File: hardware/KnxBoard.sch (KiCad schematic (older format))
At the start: 40 parts, among them J1 Conn_01x10, J2 Conn_01x12, J3 Conn_01x12, J4 Conn_01x02_Male, U1 NCN5130, U2 STM32L432KCUx, X1 FA-238

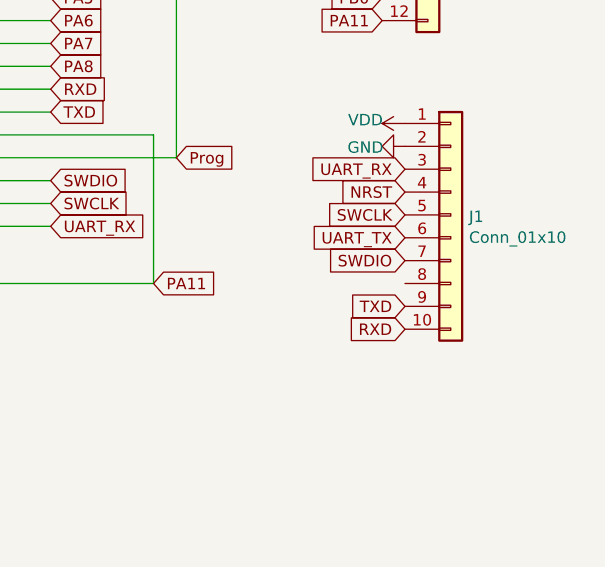
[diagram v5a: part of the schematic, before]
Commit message: update BOM prices by 10
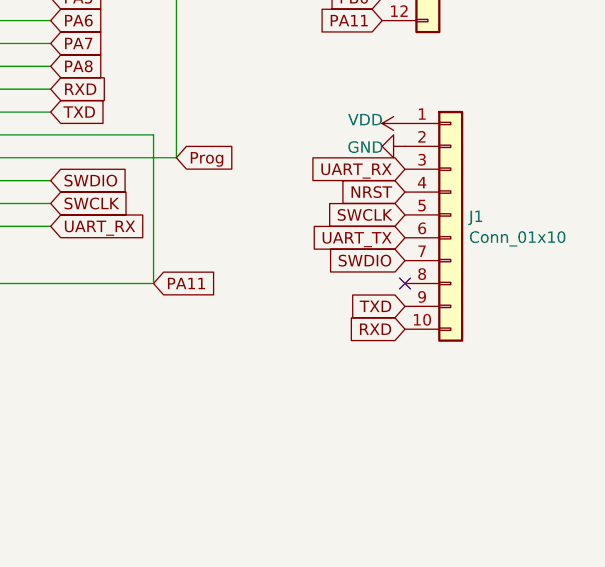
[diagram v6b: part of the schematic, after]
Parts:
- C1: Price 0.085 -> 0.021
- C10, C11, C22: Price 0.093 -> 0.039
- C2: Price 0.136 -> 0.097
- C20, C21, C23, C5, C6: Price 0.085 -> 0.026
- C3: Price 0.09 -> 0.014
- C4: Price 0.46 -> 0.353
- C41: Price 0.14 -> 0.102
- C8, C9: Price 0.085 -> 0.032
- D1: Price 0.36 -> 0.292
- D2: Price 0.3 -> 0.249
- L1, L2, L3: Price 0.15 -> 0.109
- LD1: Price 0.152 -> 0.142
- R1: Price 0.382 -> 0.285
- R22: value 0 -> NOTMOUNT
- U1: Price 7.31 -> 6.61
- U2: Price 5.8 -> 5.22
- X1: Price 0.53 -> 0.445
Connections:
- no-connect marks 2 -> 3
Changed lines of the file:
@@
 F 2 "Package_DFN_QFN:QFN-32-1EP_5x5mm_P0.5mm_EP3.45x3.45mm" H 8150 2700 50  0001 R CNN
 F 3 "https://www.mouser.fr/ProductDetail/STMicroelectronics/STM32L432KCU6?qs=sGAEpiMZZMueQxo7L%2FBPyGlkDlHQ8XwjqFkWSLh2yvA%3D" H 8550 3600 50  0001 C CNN
-F 4 "5.8" H 8550 3600 50  0001 C CNN "Price"
+F 4 "5.22" H 8550 3600 50  0001 C CNN "Price"
 	1    8550 3600
 	1    0    0    -1
@@
 F 2 "Package_DFN_QFN:QFN-40-1EP_6x6mm_P0.5mm_EP4.6x4.6mm_ThermalVias" H 3500 5300 50  0001 C CNN
 F 3 "https://www.mouser.fr/ProductDetail/onsemi/NCN5130MNTWG?qs=sGAEpiMZZMsyYdr3R27aV%2FyfBetTZLuYah%252BU%2FGK00PQ%3D" H 3150 3650 50  0001 C CNN
-F 4 "7.31" H 3150 3650 50  0001 C CNN "Price"
+F 4 "6.61" H 3150 3650 50  0001 C CNN "Price"
 	1    3150 3650
 	1    0    0    -1
@@
 F 2 "Diode_SMD:D_SMA" H 1150 3750 50  0001 C CNN
 F 3 "https://www.mouser.fr/ProductDetail/Bourns/SMAJ40CA?qs=A3H9pljuJ8S9ch8FWCUIag%3D%3D" H 1150 3750 50  0001 C CNN
-F 4 "0.3" H 1150 3750 50  0001 C CNN "Price"
+F 4 "0.249" H 1150 3750 50  0001 C CNN "Price"
 	1    1150 3750
 	0    1    1    0
@@
 F 2 "Diode_SMD:D_SMA" H 1400 3200 50  0001 C CNN
 F 3 "https://www.mouser.fr/ProductDetail/onsemi/SS16T3G?qs=xZq1yRCsb1c8788h1nFazA%3D%3D" H 1400 3200 50  0001 C CNN
-F 4 "0.36" H 1400 3200 50  0001 C CNN "Price"
+F 4 "0.292" H 1400 3200 50  0001 C CNN "Price"
 	1    1400 3200
 	-1   0    0    1
@@
 F 2 "Resistor_SMD:R_0612_1632Metric" V 2180 3200 50  0001 C CNN
 F 3 "https://www.mouser.fr/ProductDetail/KOA-Speer/WK73R2BTTD27R0F?qs=sGAEpiMZZMvdGkrng054t6odK5HnpZ6cfyF1%252BzoyWdM%3D" H 2250 3200 50  0001 C CNN
-F 4 "0.382" H 2250 3200 50  0001 C CNN "Price"
+F 4 "0.285" H 2250 3200 50  0001 C CNN "Price"
 	1    2250 3200
 	0    1    1    0
@@
 F 2 "Capacitor_SMD:C_0603_1608Metric" H 1988 3150 50  0001 C CNN
 F 3 "https://www.mouser.fr/ProductDetail/Samsung-Electro-Mechanics/CL10B473KB8NNND?qs=sGAEpiMZZMvsSlwiRhF8qlxW52pIu5FNnJM8feowB3A%3D" H 1950 3300 50  0001 C CNN
-F 4 "0.085" H 1950 3300 50  0001 C CNN "Price"
+F 4 "0.021" H 1950 3300 50  0001 C CNN "Price"
 	1    1950 3300
 	0    1    1    0
@@
 F 2 "Capacitor_SMD:C_0603_1608Metric" H 2338 3450 50  0001 C CNN
 F 3 "https://www.mouser.fr/ProductDetail/Samsung-Electro-Mechanics/CL10A224KB8NNNC?qs=sGAEpiMZZMvsSlwiRhF8qtsGU%2FCnaNeQ2pAx%2FyO8BDlqGcrTKW51Mg%3D%3D" H 2300 3600 50  0001 C CNN
-F 4 "0.136" H 2300 3600 50  0001 C CNN "Price"
+F 4 "0.097" H 2300 3600 50  0001 C CNN "Price"
 	1    2300 3600
 	0    1    1    0
@@
 F 2 "Capacitor_SMD:C_0603_1608Metric" H 1638 4000 50  0001 C CNN
 F 3 "https://www.mouser.fr/ProductDetail/Samsung-Electro-Mechanics/CL10B104KB8NFNC?qs=sGAEpiMZZMvsSlwiRhF8qunkWFWGyo%252Bv1GZw38BXXfVnkeSfSD0rvg%3D%3D" H 1600 4150 50  0001 C CNN
-F 4 "0.09" H 1600 4150 50  0001 C CNN "Price"
+F 4 "0.014" H 1600 4150 50  0001 C CNN "Price"
 	1    1600 4150
 	1    0    0    -1
@@
 F 2 "Capacitor_SMD:CP_Elec_6.3x7.7" H 1888 4000 50  0001 C CNN
 F 3 "https://www.mouser.fr/ProductDetail/Nichicon/UUR1V101MCL6GS?qs=huzeVNXgovWypttWSImRTA%3D%3D" H 1850 4150 50  0001 C CNN
-F 4 "0.46" H 1850 4150 50  0001 C CNN "Price"
+F 4 "0.353" H 1850 4150 50  0001 C CNN "Price"
 	1    1850 4150
 	1    0    0    -1
@@
 F 2 "Capacitor_SMD:C_0603_1608Metric" H 5838 3200 50  0001 C CNN
 F 3 "https://www.mouser.fr/ProductDetail/Samsung-Electro-Mechanics/CL10B104KA8NNWC?qs=sGAEpiMZZMvsSlwiRhF8qvCY8MbTG5UFsLNcvFy0oSw%3D" H 5800 3350 50  0001 C CNN
-F 4 "0.085" H 5800 3350 50  0001 C CNN "Price"
+F 4 "0.026" H 5800 3350 50  0001 C CNN "Price"
 	1    5800 3350
 	1    0    0    -1
@@
 F 2 "Capacitor_SMD:C_0603_1608Metric" H 2688 2150 50  0001 C CNN
 F 3 "https://www.mouser.fr/ProductDetail/Samsung-Electro-Mechanics/CL10B104KA8NNWC?qs=sGAEpiMZZMvsSlwiRhF8qvCY8MbTG5UFsLNcvFy0oSw%3D" H 2650 2300 50  0001 C CNN
-F 4 "0.085" H 2650 2300 50  0001 C CNN "Price"
+F 4 "0.026" H 2650 2300 50  0001 C CNN "Price"
 	1    2650 2300
 	-1   0    0    1
@@
 F 2 "Capacitor_SMD:C_0805_2012Metric" H 2638 4900 50  0001 C CNN
 F 3 "https://www.mouser.fr/ProductDetail/Samsung-Electro-Mechanics/CL21A106KOQNNNG?qs=sGAEpiMZZMvsSlwiRhF8qiamir66WTSkBRoD9MoKPnM%3D" H 2600 5050 50  0001 C CNN
-F 4 "0.093" H 2600 5050 50  0001 C CNN "Price"
+F 4 "0.039" H 2600 5050 50  0001 C CNN "Price"
 	1    2600 5050
 	1    0    0    -1
@@
 F 2 "Inductor_SMD:L_1008_2520Metric" H 3550 4850 50  0001 C CNN
 F 3 "https://www.mouser.fr/ProductDetail/Taiyo-Yuden/LB2518T221M?qs=I6KAKw0tg2yY77OJYA9jag%3D%3D" H 3550 4850 50  0001 C CNN
-F 4 "0.15" H 3550 4850 50  0001 C CNN "Price"
+F 4 "0.109" H 3550 4850 50  0001 C CNN "Price"
 	1    3550 4850
 	1    0    0    -1
@@
 F 2 "Inductor_SMD:L_1008_2520Metric" H 3750 4850 50  0001 C CNN
 F 3 "https://www.mouser.fr/ProductDetail/Taiyo-Yuden/LB2518T221M?qs=I6KAKw0tg2yY77OJYA9jag%3D%3D" H 3750 4850 50  0001 C CNN
-F 4 "0.15" H 3750 4850 50  0001 C CNN "Price"
+F 4 "0.109" H 3750 4850 50  0001 C CNN "Price"
 	1    3750 4850
 	1    0    0    -1
@@
 F 2 "Capacitor_SMD:C_0805_2012Metric" H 4388 4900 50  0001 C CNN
 F 3 "https://www.mouser.fr/ProductDetail/Samsung-Electro-Mechanics/CL21A106KOQNNNG?qs=sGAEpiMZZMvsSlwiRhF8qiamir66WTSkBRoD9MoKPnM%3D" H 4350 5050 50  0001 C CNN
-F 4 "0.093" H 4350 5050 50  0001 C CNN "Price"
+F 4 "0.039" H 4350 5050 50  0001 C CNN "Price"
 	1    4350 5050
 	1    0    0    -1
@@
 F 2 "Capacitor_SMD:C_0603_1608Metric" H 3588 1300 50  0001 C CNN
 F 3 "https://www.mouser.fr/ProductDetail/Samsung-Electro-Mechanics/CL10C100JB8NNND?qs=sGAEpiMZZMvsSlwiRhF8qlxW52pIu5FNW3qxrQ2K0NU%3D" H 3550 1450 50  0001 C CNN
-F 4 "0.085" H 3550 1450 50  0001 C CNN "Price"
+F 4 "0.032" H 3550 1450 50  0001 C CNN "Price"
 	1    3550 1450
 	1    0    0    -1
@@
 F 2 "Capacitor_SMD:C_0603_1608Metric" H 3888 1300 50  0001 C CNN
 F 3 "https://www.mouser.fr/ProductDetail/Samsung-Electro-Mechanics/CL10C100JB8NNND?qs=sGAEpiMZZMvsSlwiRhF8qlxW52pIu5FNW3qxrQ2K0NU%3D" H 3850 1450 50  0001 C CNN
-F 4 "0.085" H 3850 1450 50  0001 C CNN "Price"
+F 4 "0.032" H 3850 1450 50  0001 C CNN "Price"
 	1    3850 1450
 	1    0    0    -1
@@
 F 2 "Crystal:Crystal_SMD_SeikoEpson_FA238-4Pin_3.2x2.5mm" H 3700 1900 50  0001 C CNN
 F 3 "https://www.mouser.fr/ProductDetail/Epson-Timing/FA-238-160000MD30X-W3?qs=f9yNj16SXrIs1foPi9xf%2Fw%3D%3D" H 3700 1900 50  0001 C CNN
-F 4 "0.53" H 3700 1900 50  0001 C CNN "Price"
+F 4 "0.445" H 3700 1900 50  0001 C CNN "Price"
 	1    3700 1900
 	1    0    0    -1
@@
 F 2 "Capacitor_SMD:C_0603_1608Metric" H 2138 4000 50  0001 C CNN
 F 3 "https://www.mouser.fr/ProductDetail/Samsung-Electro-Mechanics/CL10A105KL8NNNC?qs=sGAEpiMZZMvsSlwiRhF8qtsBU8Zhqm2RLIDZDghI9lGzj%2FYVDbgmuQ%3D%3D" H 2100 4150 50  0001 C CNN
-F 4 "0.14" H 2100 4150 50  0001 C CNN "Price"
+F 4 "0.102" H 2100 4150 50  0001 C CNN "Price"
 	1    2100 4150
 	1    0    0    -1
@@
 F 2 "Capacitor_SMD:C_0603_1608Metric" H 7138 2950 50  0001 C CNN
 F 3 "https://www.mouser.fr/ProductDetail/Samsung-Electro-Mechanics/CL10B104KA8NNWC?qs=sGAEpiMZZMvsSlwiRhF8qvCY8MbTG5UFsLNcvFy0oSw%3D" H 7100 3100 50  0001 C CNN
-F 4 "0.085" H 7100 3100 50  0001 C CNN "Price"
+F 4 "0.026" H 7100 3100 50  0001 C CNN "Price"
 	1    7100 3100
 	1    0    0    -1
@@
 F 2 "Inductor_SMD:L_1008_2520Metric" H 8650 2250 50  0001 C CNN
 F 3 "https://www.mouser.fr/ProductDetail/Taiyo-Yuden/LB2518T221M?qs=I6KAKw0tg2yY77OJYA9jag%3D%3D" H 8650 2250 50  0001 C CNN
-F 4 "0.15" H 8650 2250 50  0001 C CNN "Price"
+F 4 "0.109" H 8650 2250 50  0001 C CNN "Price"
 	1    8650 2250
 	1    0    0    -1
@@
 F 2 "Capacitor_SMD:C_0603_1608Metric" H 8088 2100 50  0001 C CNN
 F 3 "https://www.mouser.fr/ProductDetail/Samsung-Electro-Mechanics/CL10B104KA8NNWC?qs=sGAEpiMZZMvsSlwiRhF8qvCY8MbTG5UFsLNcvFy0oSw%3D" H 8050 2250 50  0001 C CNN
-F 4 "0.085" H 8050 2250 50  0001 C CNN "Price"
+F 4 "0.026" H 8050 2250 50  0001 C CNN "Price"
 	1    8050 2250
 	1    0    0    -1
@@
 F 2 "Capacitor_SMD:C_0805_2012Metric" H 7838 2100 50  0001 C CNN
 F 3 "https://www.mouser.fr/ProductDetail/Samsung-Electro-Mechanics/CL21A106KOQNNNG?qs=sGAEpiMZZMvsSlwiRhF8qiamir66WTSkBRoD9MoKPnM%3D" H 7800 2250 50  0001 C CNN
-F 4 "0.093" H 7800 2250 50  0001 C CNN "Price"
+F 4 "0.039" H 7800 2250 50  0001 C CNN "Price"
 	1    7800 2250
 	1    0    0    -1
@@
 F 2 "LED_SMD:LED_0603_1608Metric" H 6950 4000 50  0001 C CNN
 F 3 "https://www.mouser.fr/ProductDetail/Wurth-Elektronik/150060RS55040?qs=8Aam6%252B7C6HHnMZFlrlTntA%3D%3D" H 6950 4000 50  0001 C CNN
-F 4 "0.152" H 6950 4000 50  0001 C CNN "Price"
+F 4 "0.142" H 6950 4000 50  0001 C CNN "Price"
 	1    6950 4000
 	1    0    0    -1
@@
 F 2 "Capacitor_SMD:C_0603_1608Metric" H 9638 2250 50  0001 C CNN
 F 3 "https://www.mouser.fr/ProductDetail/Samsung-Electro-Mechanics/CL10B104KA8NNWC?qs=sGAEpiMZZMvsSlwiRhF8qvCY8MbTG5UFsLNcvFy0oSw%3D" H 9600 2400 50  0001 C CNN
-F 4 "0.085" H 9600 2400 50  0001 C CNN "Price"
+F 4 "0.026" H 9600 2400 50  0001 C CNN "Price"
 	1    9600 2400
 	1    0    0    -1
@@
 P 6400 2450
 F 0 "R22" V 6285 2450 50  0000 C CNN
-F 1 "0" V 6284 2450 50  0001 C CNN
+F 1 "NOTMOUNT" V 6284 2450 50  0001 C CNN
 F 2 "Resistor_SMD:R_0603_1608Metric" V 6330 2450 50  0001 C CNN
 F 3 "~" H 6400 2450 50  0001 C CNN
@@
 Wire Wire Line
 	6550 2450 7100 2450
+NoConn ~ 10850 4650
 $EndSCHEMATC

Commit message: Add MPN in BOM
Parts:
- C1: MPN (none) -> CL10B473KB8NNND
- C10, C11, C22: MPN (none) -> CL21A106KOQNNNG
- C2: MPN (none) -> CL10A224KB8NNNC
- C20, C21, C23, C5, C6: MPN (none) -> CL10B104KA8NNWC
- C3: MPN (none) -> CL10B104KB8NFNC
- C4: MPN (none) -> UUR1V101MCL6GS
- C41: MPN (none) -> CL10A105KL8NNNC
- C8, C9: MPN (none) -> CL10C100JB8NNND
- D1: MPN (none) -> SS16T3G
- D2: MPN (none) -> SMAJ40CA
- L1, L2, L3: MPN (none) -> LB2518T221M
- LD1: MPN (none) -> 150060RS55040
- R1: MPN (none) -> WK73R2BTTD27R0F
- R2, R3: MPN (none) -> CRCW06031R00JNEC
- R20: MPN (none) -> MCT06030C1002FP500
- R21: MPN (none) -> MCT06030C1000FP500
- R4: MPN (none) -> MCT06030C5602FP500
- R5: MPN (none) -> MCT06030C4993FP500
- SwProg1, SwReset1: MPN (none) -> SKQGABE010
- U1: MPN (none) -> NCN5130MNTWG
- U2: MPN (none) -> STM32L432KCU6
- X1: MPN (none) -> FA-238 16.0000MD30X-W3
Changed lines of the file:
@@
 F 3 "https://www.mouser.fr/ProductDetail/STMicroelectronics/STM32L432KCU6?qs=sGAEpiMZZMueQxo7L%2FBPyGlkDlHQ8XwjqFkWSLh2yvA%3D" H 8550 3600 50  0001 C CNN
 F 4 "5.22" H 8550 3600 50  0001 C CNN "Price"
+F 5 "STM32L432KCU6 " H 8550 3600 50  0001 C CNN "MPN"
 	1    8550 3600
 	1    0    0    -1
@@
 F 3 "https://www.mouser.fr/ProductDetail/onsemi/NCN5130MNTWG?qs=sGAEpiMZZMsyYdr3R27aV%2FyfBetTZLuYah%252BU%2FGK00PQ%3D" H 3150 3650 50  0001 C CNN
 F 4 "6.61" H 3150 3650 50  0001 C CNN "Price"
+F 5 "NCN5130MNTWG " H 3150 3650 50  0001 C CNN "MPN"
 	1    3150 3650
 	1    0    0    -1
@@
 F 3 "https://www.mouser.fr/ProductDetail/Bourns/SMAJ40CA?qs=A3H9pljuJ8S9ch8FWCUIag%3D%3D" H 1150 3750 50  0001 C CNN
 F 4 "0.249" H 1150 3750 50  0001 C CNN "Price"
+F 5 "SMAJ40CA " H 1150 3750 50  0001 C CNN "MPN"
 	1    1150 3750
 	0    1    1    0
@@
 F 3 "https://www.mouser.fr/ProductDetail/onsemi/SS16T3G?qs=xZq1yRCsb1c8788h1nFazA%3D%3D" H 1400 3200 50  0001 C CNN
 F 4 "0.292" H 1400 3200 50  0001 C CNN "Price"
+F 5 "SS16T3G " H 1400 3200 50  0001 C CNN "MPN"
 	1    1400 3200
 	-1   0    0    1
@@
 F 3 "https://www.mouser.fr/ProductDetail/KOA-Speer/WK73R2BTTD27R0F?qs=sGAEpiMZZMvdGkrng054t6odK5HnpZ6cfyF1%252BzoyWdM%3D" H 2250 3200 50  0001 C CNN
 F 4 "0.285" H 2250 3200 50  0001 C CNN "Price"
+F 5 "WK73R2BTTD27R0F " H 2250 3200 50  0001 C CNN "MPN"
 	1    2250 3200
 	0    1    1    0
@@
 F 3 "https://www.mouser.fr/ProductDetail/Samsung-Electro-Mechanics/CL10B473KB8NNND?qs=sGAEpiMZZMvsSlwiRhF8qlxW52pIu5FNnJM8feowB3A%3D" H 1950 3300 50  0001 C CNN
 F 4 "0.021" H 1950 3300 50  0001 C CNN "Price"
+F 5 "CL10B473KB8NNND " H 1950 3300 50  0001 C CNN "MPN"
 	1    1950 3300
 	0    1    1    0
@@
 F 3 "https://www.mouser.fr/ProductDetail/Samsung-Electro-Mechanics/CL10A224KB8NNNC?qs=sGAEpiMZZMvsSlwiRhF8qtsGU%2FCnaNeQ2pAx%2FyO8BDlqGcrTKW51Mg%3D%3D" H 2300 3600 50  0001 C CNN
 F 4 "0.097" H 2300 3600 50  0001 C CNN "Price"
+F 5 "CL10A224KB8NNNC " H 2300 3600 50  0001 C CNN "MPN"
 	1    2300 3600
 	0    1    1    0
@@
 F 3 "https://www.mouser.fr/ProductDetail/Samsung-Electro-Mechanics/CL10B104KB8NFNC?qs=sGAEpiMZZMvsSlwiRhF8qunkWFWGyo%252Bv1GZw38BXXfVnkeSfSD0rvg%3D%3D" H 1600 4150 50  0001 C CNN
 F 4 "0.014" H 1600 4150 50  0001 C CNN "Price"
+F 5 "CL10B104KB8NFNC " H 1600 4150 50  0001 C CNN "MPN"
 	1    1600 4150
 	1    0    0    -1
@@
 F 3 "https://www.mouser.fr/ProductDetail/Nichicon/UUR1V101MCL6GS?qs=huzeVNXgovWypttWSImRTA%3D%3D" H 1850 4150 50  0001 C CNN
 F 4 "0.353" H 1850 4150 50  0001 C CNN "Price"
+F 5 "UUR1V101MCL6GS " H 1850 4150 50  0001 C CNN "MPN"
 	1    1850 4150
 	1    0    0    -1
@@
 F 3 "https://www.mouser.fr/ProductDetail/Samsung-Electro-Mechanics/CL10B104KA8NNWC?qs=sGAEpiMZZMvsSlwiRhF8qvCY8MbTG5UFsLNcvFy0oSw%3D" H 5800 3350 50  0001 C CNN
 F 4 "0.026" H 5800 3350 50  0001 C CNN "Price"
+F 5 "CL10B104KA8NNWC " H 5800 3350 50  0001 C CNN "MPN"
 	1    5800 3350
 	1    0    0    -1
@@
 F 3 "https://www.mouser.fr/ProductDetail/Samsung-Electro-Mechanics/CL10B104KA8NNWC?qs=sGAEpiMZZMvsSlwiRhF8qvCY8MbTG5UFsLNcvFy0oSw%3D" H 2650 2300 50  0001 C CNN
 F 4 "0.026" H 2650 2300 50  0001 C CNN "Price"
+F 5 "CL10B104KA8NNWC " H 2650 2300 50  0001 C CNN "MPN"
 	1    2650 2300
 	-1   0    0    1
@@
 F 3 "https://www.mouser.fr/ProductDetail/Samsung-Electro-Mechanics/CL21A106KOQNNNG?qs=sGAEpiMZZMvsSlwiRhF8qiamir66WTSkBRoD9MoKPnM%3D" H 2600 5050 50  0001 C CNN
 F 4 "0.039" H 2600 5050 50  0001 C CNN "Price"
+F 5 "CL21A106KOQNNNG " H 2600 5050 50  0001 C CNN "MPN"
 	1    2600 5050
 	1    0    0    -1
@@
 F 3 "https://www.mouser.fr/ProductDetail/Vishay-Beyschlag/MCT06030C5602FP500?qs=sGAEpiMZZMvdGkrng054txcf3av6vnC8XzTnB3mS7jw%3D" H 2900 4750 50  0001 C CNN
 F 4 "0.08" H 2900 4750 50  0001 C CNN "Price"
+F 5 "MCT06030C5602FP500 " H 2900 4750 50  0001 C CNN "MPN"
 	1    2900 4750
 	-1   0    0    1
@@
 F 3 "https://www.mouser.fr/ProductDetail/Vishay-Beyschlag/MCT06030C4993FP500?qs=8lczJKL2ryeXiIiBeB6JCA%3D%3D" H 2900 5250 50  0001 C CNN
 F 4 "0.102" H 2900 5250 50  0001 C CNN "Price"
+F 5 "MCT06030C4993FP500 " H 2900 5250 50  0001 C CNN "MPN"
 	1    2900 5250
 	-1   0    0    1
@@
 F 3 "https://www.mouser.fr/ProductDetail/Vishay-Dale/CRCW06031R00JNEC?qs=sGAEpiMZZMvdGkrng054t8tsKUCh5%2FbY4AhBMsyzAQQ%3D" H 3350 4850 50  0001 C CNN
 F 4 "0.008" H 3350 4850 50  0001 C CNN "Price"
+F 5 "CRCW06031R00JNEC " H 3350 4850 50  0001 C CNN "MPN"
 	1    3350 4850
 	-1   0    0    1
@@
 F 3 "https://www.mouser.fr/ProductDetail/Taiyo-Yuden/LB2518T221M?qs=I6KAKw0tg2yY77OJYA9jag%3D%3D" H 3550 4850 50  0001 C CNN
 F 4 "0.109" H 3550 4850 50  0001 C CNN "Price"
+F 5 "LB2518T221M " H 3550 4850 50  0001 C CNN "MPN"
 	1    3550 4850
 	1    0    0    -1
@@
 F 3 "https://www.mouser.fr/ProductDetail/Taiyo-Yuden/LB2518T221M?qs=I6KAKw0tg2yY77OJYA9jag%3D%3D" H 3750 4850 50  0001 C CNN
 F 4 "0.109" H 3750 4850 50  0001 C CNN "Price"
+F 5 "LB2518T221M " H 3750 4850 50  0001 C CNN "MPN"
 	1    3750 4850
 	1    0    0    -1
@@
 F 3 "https://www.mouser.fr/ProductDetail/Vishay-Dale/CRCW06031R00JNEC?qs=sGAEpiMZZMvdGkrng054t8tsKUCh5%2FbY4AhBMsyzAQQ%3D" H 3950 4850 50  0001 C CNN
 F 4 "0.008" H 3950 4850 50  0001 C CNN "Price"
+F 5 "CRCW06031R00JNEC " H 3950 4850 50  0001 C CNN "MPN"
 	1    3950 4850
 	-1   0    0    1
@@
 F 3 "https://www.mouser.fr/ProductDetail/Samsung-Electro-Mechanics/CL21A106KOQNNNG?qs=sGAEpiMZZMvsSlwiRhF8qiamir66WTSkBRoD9MoKPnM%3D" H 4350 5050 50  0001 C CNN
 F 4 "0.039" H 4350 5050 50  0001 C CNN "Price"
+F 5 "CL21A106KOQNNNG " H 4350 5050 50  0001 C CNN "MPN"
 	1    4350 5050
 	1    0    0    -1
@@
 F 3 "https://www.mouser.fr/ProductDetail/Samsung-Electro-Mechanics/CL10C100JB8NNND?qs=sGAEpiMZZMvsSlwiRhF8qlxW52pIu5FNW3qxrQ2K0NU%3D" H 3550 1450 50  0001 C CNN
 F 4 "0.032" H 3550 1450 50  0001 C CNN "Price"
+F 5 "CL10C100JB8NNND " H 3550 1450 50  0001 C CNN "MPN"
 	1    3550 1450
 	1    0    0    -1
@@
 F 3 "https://www.mouser.fr/ProductDetail/Samsung-Electro-Mechanics/CL10C100JB8NNND?qs=sGAEpiMZZMvsSlwiRhF8qlxW52pIu5FNW3qxrQ2K0NU%3D" H 3850 1450 50  0001 C CNN
 F 4 "0.032" H 3850 1450 50  0001 C CNN "Price"
+F 5 "CL10C100JB8NNND " H 3850 1450 50  0001 C CNN "MPN"
 	1    3850 1450
 	1    0    0    -1
@@
 F 3 "https://www.mouser.fr/ProductDetail/Epson-Timing/FA-238-160000MD30X-W3?qs=f9yNj16SXrIs1foPi9xf%2Fw%3D%3D" H 3700 1900 50  0001 C CNN
 F 4 "0.445" H 3700 1900 50  0001 C CNN "Price"
+F 5 "FA-238 16.0000MD30X-W3 " H 3700 1900 50  0001 C CNN "MPN"
 	1    3700 1900
 	1    0    0    -1
@@
 F 3 "https://www.mouser.fr/ProductDetail/Samsung-Electro-Mechanics/CL10A105KL8NNNC?qs=sGAEpiMZZMvsSlwiRhF8qtsBU8Zhqm2RLIDZDghI9lGzj%2FYVDbgmuQ%3D%3D" H 2100 4150 50  0001 C CNN
 F 4 "0.102" H 2100 4150 50  0001 C CNN "Price"
+F 5 "CL10A105KL8NNNC " H 2100 4150 50  0001 C CNN "MPN"
 	1    2100 4150
 	1    0    0    -1
@@
 F 3 "https://www.mouser.fr/ProductDetail/Samsung-Electro-Mechanics/CL10B104KA8NNWC?qs=sGAEpiMZZMvsSlwiRhF8qvCY8MbTG5UFsLNcvFy0oSw%3D" H 7100 3100 50  0001 C CNN
 F 4 "0.026" H 7100 3100 50  0001 C CNN "Price"
+F 5 "CL10B104KA8NNWC " H 7100 3100 50  0001 C CNN "MPN"
 	1    7100 3100
 	1    0    0    -1
@@
 F 3 "https://www.mouser.fr/ProductDetail/ALPS/SKQGABE010?qs=N5Jky1br14NGdH0AMYxewQ%3D%3D" H 7450 3300 50  0001 C CNN
 F 4 "0.497" H 7450 3100 50  0001 C CNN "Price"
+F 5 "SKQGABE010 " H 7450 3100 50  0001 C CNN "MPN"
 	1    7450 3100
 	0    1    1    0
@@
 F 3 "https://www.mouser.fr/ProductDetail/Vishay-Beyschlag/MCT06030C1002FP500?qs=sGAEpiMZZMvdGkrng054t%252B7N8nKX0VXe%2FafJHKs0Nqw%3D" H 7750 3300 50  0001 C CNN
 F 4 "0.085" H 7750 3300 50  0001 C CNN "Price"
+F 5 "MCT06030C1002FP500 " H 7750 3300 50  0001 C CNN "MPN"
 	1    7750 3300
 	0    1    1    0
@@
 F 3 "https://www.mouser.fr/ProductDetail/Taiyo-Yuden/LB2518T221M?qs=I6KAKw0tg2yY77OJYA9jag%3D%3D" H 8650 2250 50  0001 C CNN
 F 4 "0.109" H 8650 2250 50  0001 C CNN "Price"
+F 5 "LB2518T221M " H 8650 2250 50  0001 C CNN "MPN"
 	1    8650 2250
 	1    0    0    -1
@@
 F 3 "https://www.mouser.fr/ProductDetail/Samsung-Electro-Mechanics/CL10B104KA8NNWC?qs=sGAEpiMZZMvsSlwiRhF8qvCY8MbTG5UFsLNcvFy0oSw%3D" H 8050 2250 50  0001 C CNN
 F 4 "0.026" H 8050 2250 50  0001 C CNN "Price"
+F 5 "CL10B104KA8NNWC " H 8050 2250 50  0001 C CNN "MPN"
 	1    8050 2250
 	1    0    0    -1
@@
 F 3 "https://www.mouser.fr/ProductDetail/Samsung-Electro-Mechanics/CL21A106KOQNNNG?qs=sGAEpiMZZMvsSlwiRhF8qiamir66WTSkBRoD9MoKPnM%3D" H 7800 2250 50  0001 C CNN
 F 4 "0.039" H 7800 2250 50  0001 C CNN "Price"
+F 5 "CL21A106KOQNNNG " H 7800 2250 50  0001 C CNN "MPN"
 	1    7800 2250
 	1    0    0    -1
@@
 F 3 "https://www.mouser.fr/ProductDetail/Vishay-Beyschlag/MCT06030C1000FP500?qs=sGAEpiMZZMvdGkrng054t%252B7APogc7nBOr0El19B1Nr8%3D" H 7500 4000 50  0001 C CNN
 F 4 "0.075" H 7500 4000 50  0001 C CNN "Price"
+F 5 "MCT06030C1000FP500 " H 7500 4000 50  0001 C CNN "MPN"
 	1    7500 4000
 	0    1    1    0
@@
 F 3 "https://www.mouser.fr/ProductDetail/Wurth-Elektronik/150060RS55040?qs=8Aam6%252B7C6HHnMZFlrlTntA%3D%3D" H 6950 4000 50  0001 C CNN
 F 4 "0.142" H 6950 4000 50  0001 C CNN "Price"
+F 5 "150060RS55040 " H 6950 4000 50  0001 C CNN "MPN"
 	1    6950 4000
 	1    0    0    -1
@@
 F 3 "https://www.mouser.fr/ProductDetail/ALPS/SKQGABE010?qs=N5Jky1br14NGdH0AMYxewQ%3D%3D" H 9850 2600 50  0001 C CNN
 F 4 "0.497" H 9850 2400 50  0001 C CNN "Price"
+F 5 "SKQGABE010 " H 9850 2400 50  0001 C CNN "MPN"
 	1    9850 2400
 	0    1    1    0
@@
 F 3 "https://www.mouser.fr/ProductDetail/Samsung-Electro-Mechanics/CL10B104KA8NNWC?qs=sGAEpiMZZMvsSlwiRhF8qvCY8MbTG5UFsLNcvFy0oSw%3D" H 9600 2400 50  0001 C CNN
 F 4 "0.026" H 9600 2400 50  0001 C CNN "Price"
+F 5 "CL10B104KA8NNWC " H 9600 2400 50  0001 C CNN "MPN"
 	1    9600 2400
 	1    0    0    -1
